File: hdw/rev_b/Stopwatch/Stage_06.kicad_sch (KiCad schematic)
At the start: 5 parts

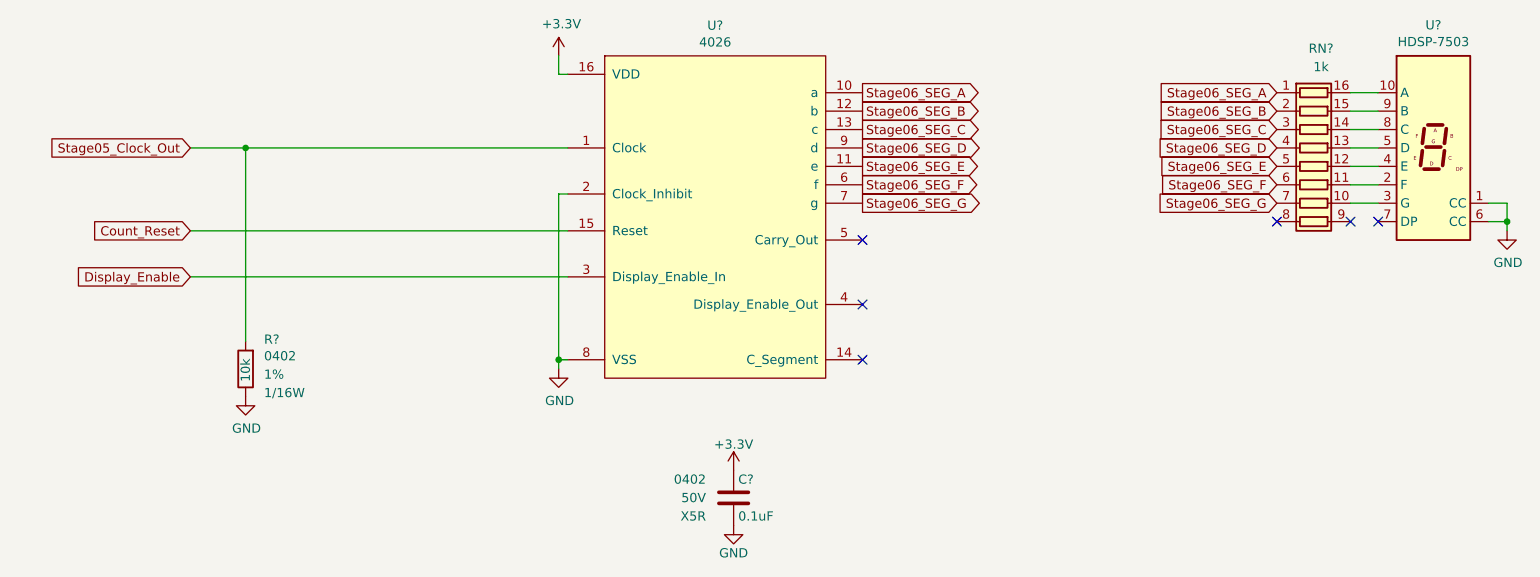
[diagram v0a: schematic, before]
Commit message: ported rev b to kicad 8
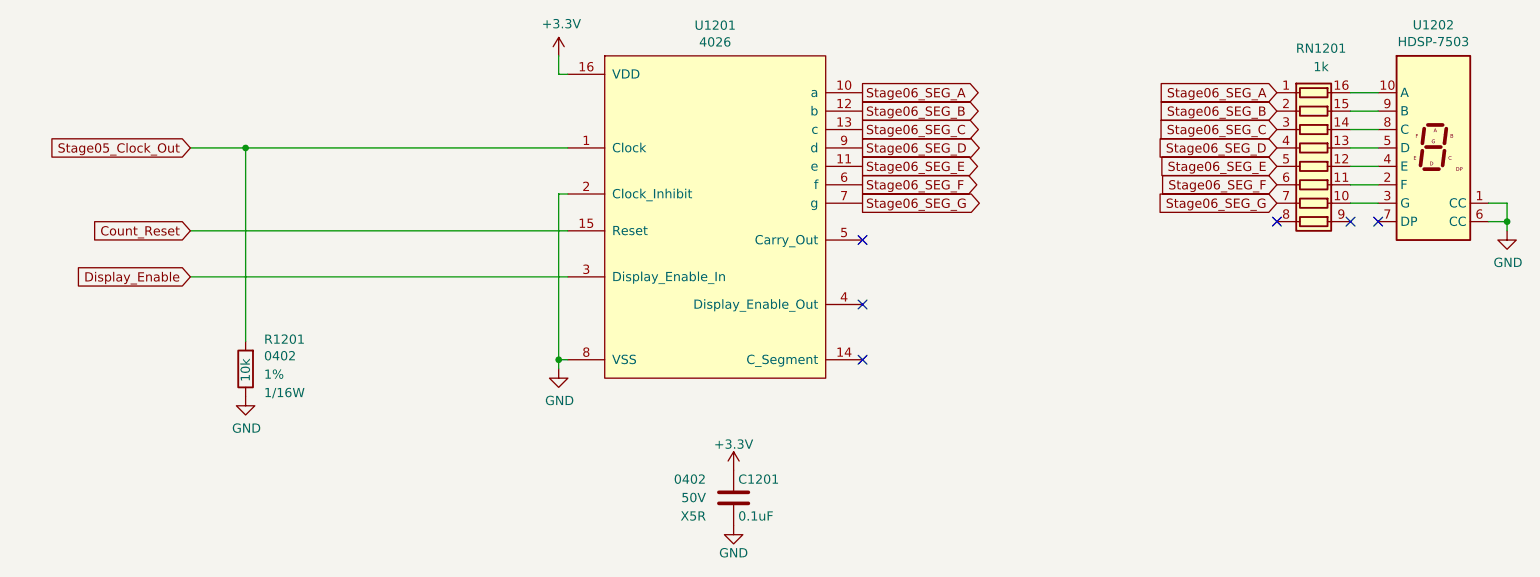
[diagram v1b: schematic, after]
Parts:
- gave numbers to parts that had none: 5
